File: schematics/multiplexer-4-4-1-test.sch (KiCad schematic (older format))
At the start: 10 parts

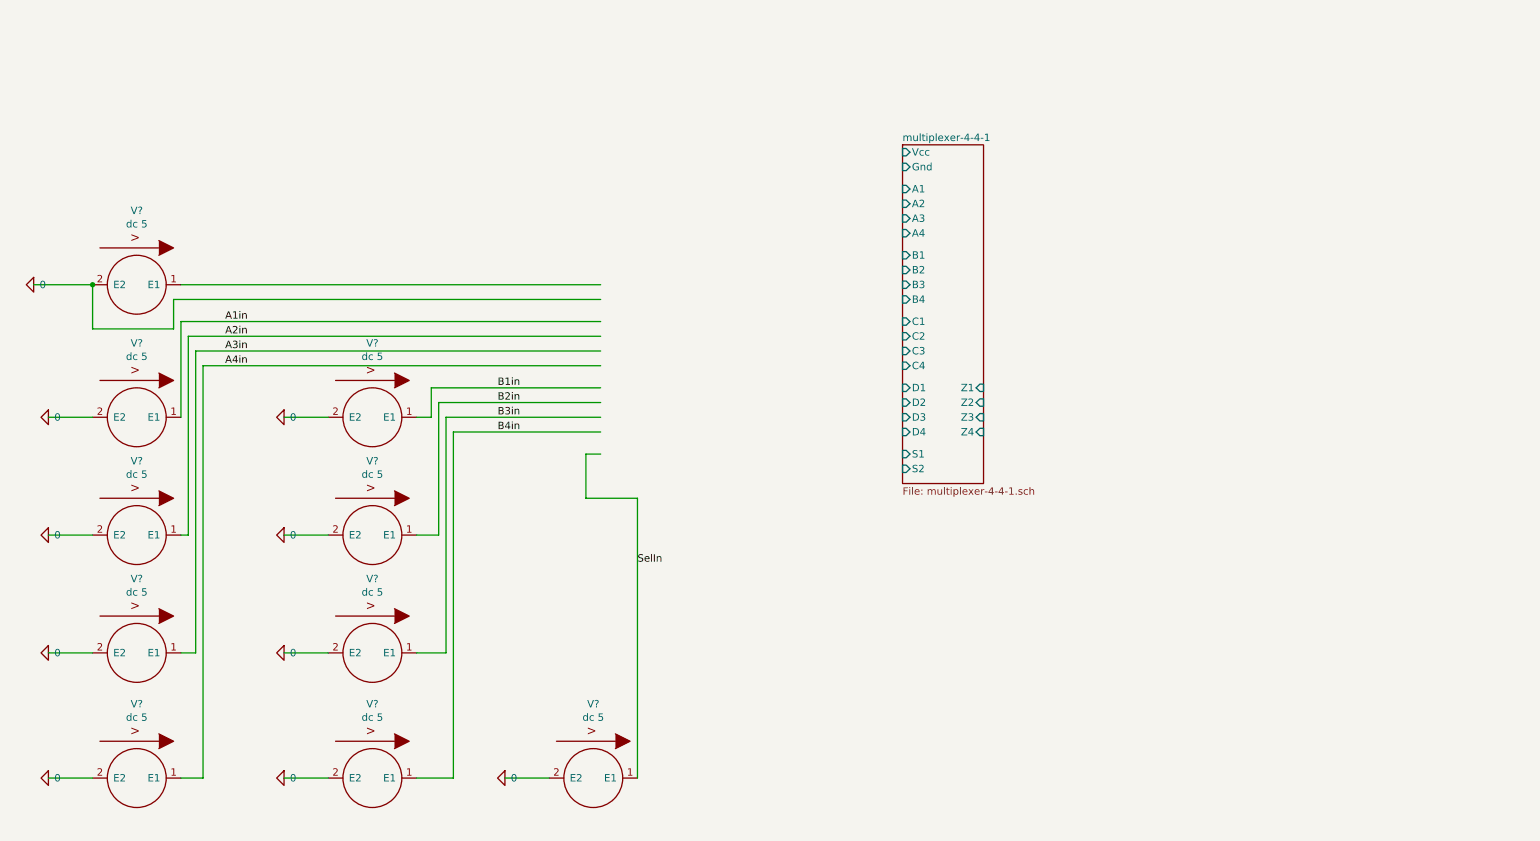
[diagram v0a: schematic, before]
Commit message: Adds a test for the 4-4-1 multiplexer
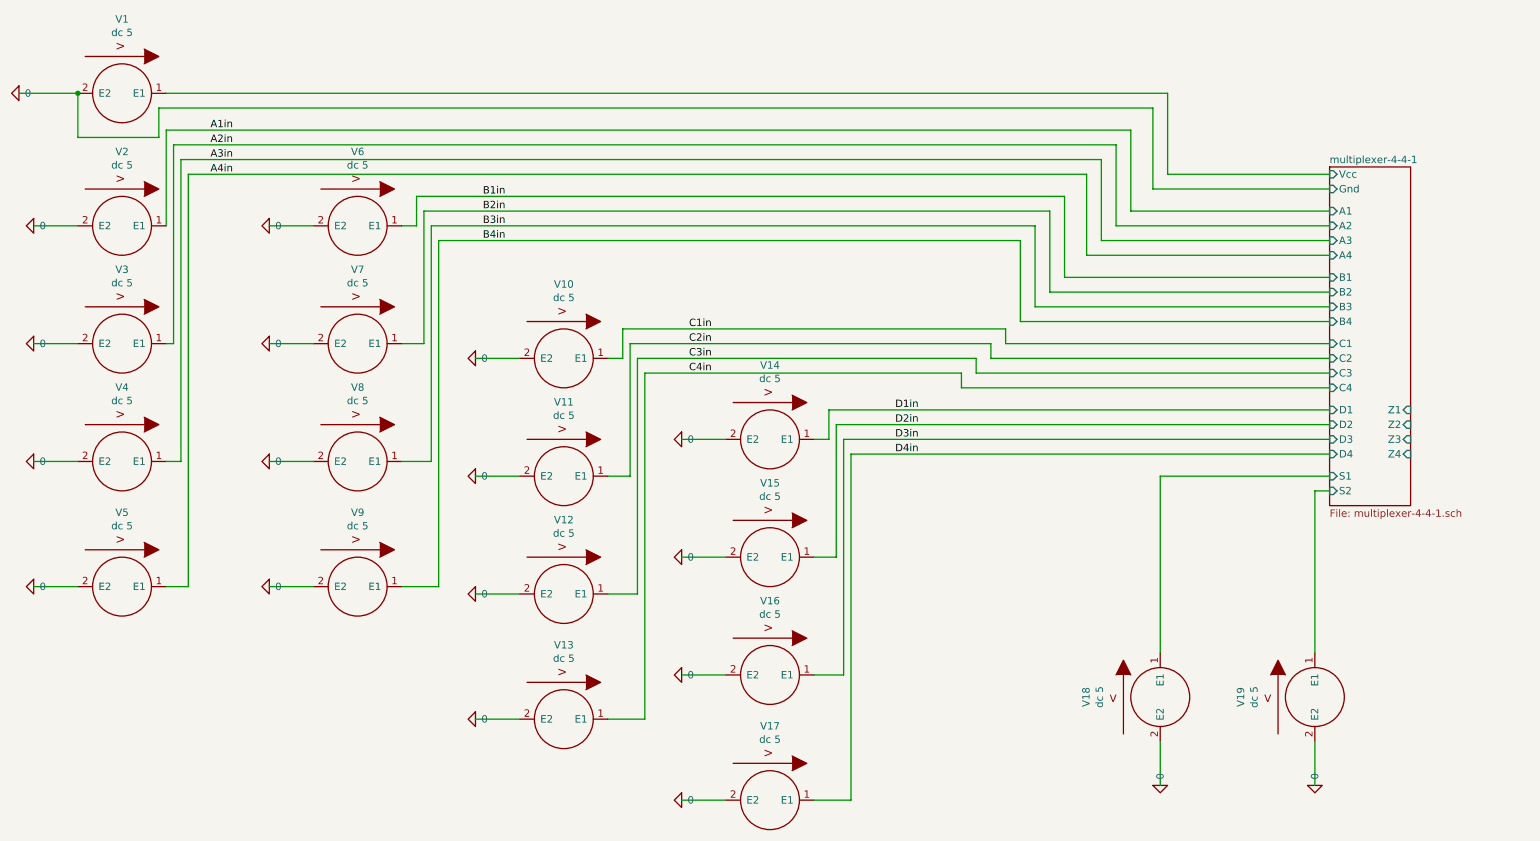
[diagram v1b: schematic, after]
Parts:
- added V10, V11, V12, V13, V14, V15, V16, V17, V19: dc 5, symbol pspice:VSOURCE
- gave numbers to parts that had none: 10
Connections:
- net labels added: C1in, C2in, C3in, C4in, D1in, D2in, D3in, D4in
- net labels removed: SelIn
- wire segments 42 -> 103
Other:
- moved on the sheet: V1, V18, V2, V3, V4, V5, V6, V7, V8, V9

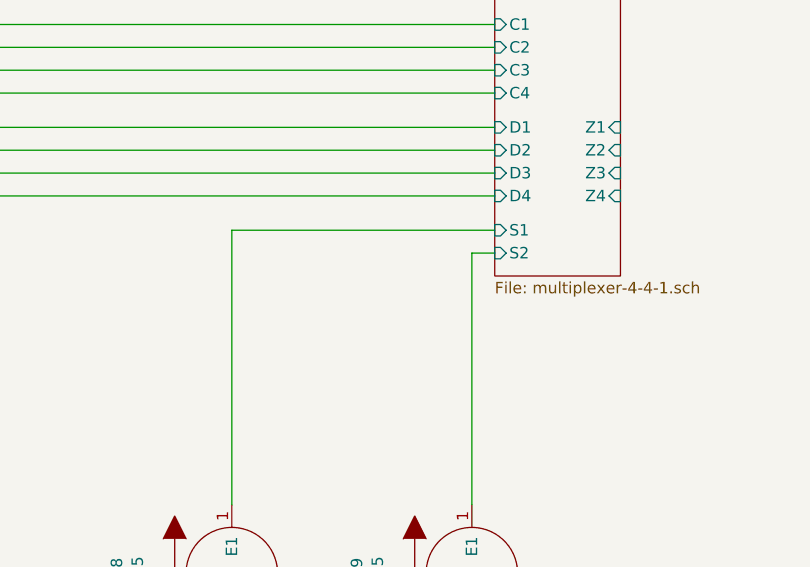
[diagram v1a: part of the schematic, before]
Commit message: More testing.  Trying to find defect in ALU
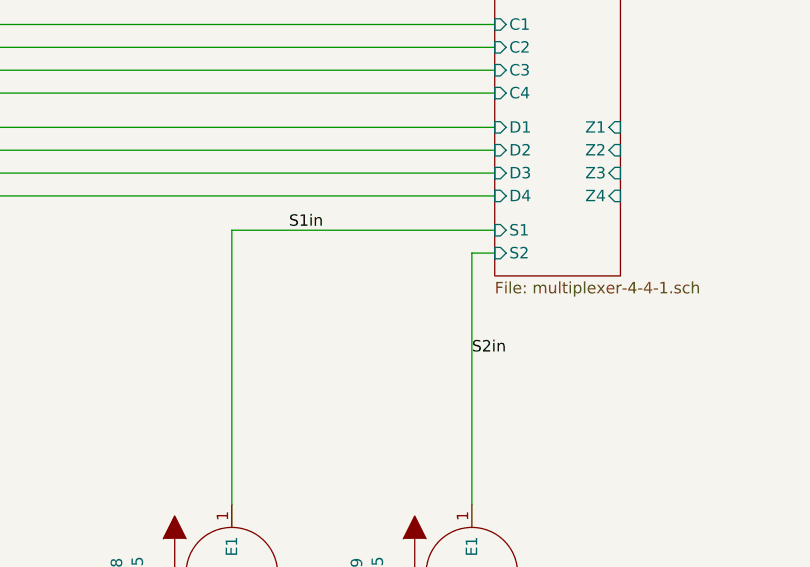
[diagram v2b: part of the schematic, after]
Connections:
- net multiplexer-4-4-1/S1 renamed S1in
- net multiplexer-4-4-1/S2 renamed S2in
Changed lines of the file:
@@
 EESchema Schematic File Version 4
+LIBS:multiplexer-4-4-1-test-cache
 EELAYER 26 0
 EELAYER END
@@
 P 950 1400
 AR Path="/5C44C753/5C44D98D" Ref="#GND?"  Part="1"
-AR Path="/5C44D98D" Ref="#GND0101"  Part="1"
-F 0 "#GND0101" H 950 1300 50  0001 C CNN
+AR Path="/5C44D98D" Ref="#GND01"  Part="1"
+F 0 "#GND01" H 950 1300 50  0001 C CNN
 F 1 "0" V 950 1440 50  0000 L CNN
 F 2 "" H 950 1400 50  0001 C CNN
@@
 P 1050 2300
 AR Path="/5C44C753/5C44D9A0" Ref="#GND?"  Part="1"
-AR Path="/5C44D9A0" Ref="#GND0102"  Part="1"
-F 0 "#GND0102" H 1050 2200 50  0001 C CNN
+AR Path="/5C44D9A0" Ref="#GND02"  Part="1"
+F 0 "#GND02" H 1050 2200 50  0001 C CNN
 F 1 "0" V 1050 2340 50  0000 L CNN
 F 2 "" H 1050 2300 50  0001 C CNN
@@
 P 1050 3100
 AR Path="/5C44C753/5C44D9AE" Ref="#GND?"  Part="1"
-AR Path="/5C44D9AE" Ref="#GND0103"  Part="1"
-F 0 "#GND0103" H 1050 3000 50  0001 C CNN
+AR Path="/5C44D9AE" Ref="#GND03"  Part="1"
+F 0 "#GND03" H 1050 3000 50  0001 C CNN
 F 1 "0" V 1050 3140 50  0000 L CNN
 F 2 "" H 1050 3100 50  0001 C CNN
@@
 P 1050 3900
 AR Path="/5C44C753/5C44D9BC" Ref="#GND?"  Part="1"
-AR Path="/5C44D9BC" Ref="#GND0104"  Part="1"
-F 0 "#GND0104" H 1050 3800 50  0001 C CNN
+AR Path="/5C44D9BC" Ref="#GND04"  Part="1"
+F 0 "#GND04" H 1050 3800 50  0001 C CNN
 F 1 "0" V 1050 3940 50  0000 L CNN
 F 2 "" H 1050 3900 50  0001 C CNN
@@
 P 1050 4750
 AR Path="/5C44C753/5C44D9CA" Ref="#GND?"  Part="1"
-AR Path="/5C44D9CA" Ref="#GND0105"  Part="1"
-F 0 "#GND0105" H 1050 4650 50  0001 C CNN
+AR Path="/5C44D9CA" Ref="#GND05"  Part="1"
+F 0 "#GND05" H 1050 4650 50  0001 C CNN
 F 1 "0" V 1050 4790 50  0000 L CNN
 F 2 "" H 1050 4750 50  0001 C CNN
@@
 P 2650 4750
 AR Path="/5C44C753/5C44D9D8" Ref="#GND?"  Part="1"
-AR Path="/5C44D9D8" Ref="#GND0106"  Part="1"
-F 0 "#GND0106" H 2650 4650 50  0001 C CNN
+AR Path="/5C44D9D8" Ref="#GND09"  Part="1"
+F 0 "#GND09" H 2650 4650 50  0001 C CNN
 F 1 "0" V 2650 4790 50  0000 L CNN
 F 2 "" H 2650 4750 50  0001 C CNN
@@
 P 2650 3900
 AR Path="/5C44C753/5C44D9E6" Ref="#GND?"  Part="1"
-AR Path="/5C44D9E6" Ref="#GND0107"  Part="1"
-F 0 "#GND0107" H 2650 3800 50  0001 C CNN
+AR Path="/5C44D9E6" Ref="#GND08"  Part="1"
+F 0 "#GND08" H 2650 3800 50  0001 C CNN
 F 1 "0" V 2650 3940 50  0000 L CNN
 F 2 "" H 2650 3900 50  0001 C CNN
@@
 P 2650 3100
 AR Path="/5C44C753/5C44D9F4" Ref="#GND?"  Part="1"
-AR Path="/5C44D9F4" Ref="#GND0108"  Part="1"
-F 0 "#GND0108" H 2650 3000 50  0001 C CNN
+AR Path="/5C44D9F4" Ref="#GND07"  Part="1"
+F 0 "#GND07" H 2650 3000 50  0001 C CNN
 F 1 "0" V 2650 3140 50  0000 L CNN
 F 2 "" H 2650 3100 50  0001 C CNN
@@
 P 2650 2300
 AR Path="/5C44C753/5C44DA02" Ref="#GND?"  Part="1"
-AR Path="/5C44DA02" Ref="#GND0109"  Part="1"
-F 0 "#GND0109" H 2650 2200 50  0001 C CNN
+AR Path="/5C44DA02" Ref="#GND06"  Part="1"
+F 0 "#GND06" H 2650 2200 50  0001 C CNN
 F 1 "0" V 2650 2340 50  0000 L CNN
 F 2 "" H 2650 2300 50  0001 C CNN
@@
 P 8700 6100
 AR Path="/5C44C753/5C44DA10" Ref="#GND?"  Part="1"
-AR Path="/5C44DA10" Ref="#GND0110"  Part="1"
-F 0 "#GND0110" H 8700 6000 50  0001 C CNN
+AR Path="/5C44DA10" Ref="#GND018"  Part="1"
+F 0 "#GND018" H 8700 6000 50  0001 C CNN
 F 1 "0" V 8700 6140 50  0000 L CNN
 F 2 "" H 8700 6100 50  0001 C CNN
@@
 P 4050 5650
 AR Path="/5C44C753/5C4656F5" Ref="#GND?"  Part="1"
-AR Path="/5C4656F5" Ref="#GND0111"  Part="1"
-F 0 "#GND0111" H 4050 5550 50  0001 C CNN
+AR Path="/5C4656F5" Ref="#GND013"  Part="1"
+F 0 "#GND013" H 4050 5550 50  0001 C CNN
 F 1 "0" V 4050 5690 50  0000 L CNN
 F 2 "" H 4050 5650 50  0001 C CNN
@@
 P 4050 4800
 AR Path="/5C44C753/5C465703" Ref="#GND?"  Part="1"
-AR Path="/5C465703" Ref="#GND0112"  Part="1"
-F 0 "#GND0112" H 4050 4700 50  0001 C CNN
+AR Path="/5C465703" Ref="#GND012"  Part="1"
+F 0 "#GND012" H 4050 4700 50  0001 C CNN
 F 1 "0" V 4050 4840 50  0000 L CNN
 F 2 "" H 4050 4800 50  0001 C CNN
@@
 P 4050 4000
 AR Path="/5C44C753/5C465711" Ref="#GND?"  Part="1"
-AR Path="/5C465711" Ref="#GND0113"  Part="1"
-F 0 "#GND0113" H 4050 3900 50  0001 C CNN
+AR Path="/5C465711" Ref="#GND011"  Part="1"
+F 0 "#GND011" H 4050 3900 50  0001 C CNN
 F 1 "0" V 4050 4040 50  0000 L CNN
 F 2 "" H 4050 4000 50  0001 C CNN
@@
 P 4050 3200
 AR Path="/5C44C753/5C46571F" Ref="#GND?"  Part="1"
-AR Path="/5C46571F" Ref="#GND0114"  Part="1"
-F 0 "#GND0114" H 4050 3100 50  0001 C CNN
+AR Path="/5C46571F" Ref="#GND010"  Part="1"
+F 0 "#GND010" H 4050 3100 50  0001 C CNN
 F 1 "0" V 4050 3240 50  0000 L CNN
 F 2 "" H 4050 3200 50  0001 C CNN
@@
 P 5450 6200
 AR Path="/5C44C753/5C467250" Ref="#GND?"  Part="1"
-AR Path="/5C467250" Ref="#GND0115"  Part="1"
-F 0 "#GND0115" H 5450 6100 50  0001 C CNN
+AR Path="/5C467250" Ref="#GND017"  Part="1"
+F 0 "#GND017" H 5450 6100 50  0001 C CNN
 F 1 "0" V 5450 6240 50  0000 L CNN
 F 2 "" H 5450 6200 50  0001 C CNN
@@
 P 5450 5350
 AR Path="/5C44C753/5C46725E" Ref="#GND?"  Part="1"
-AR Path="/5C46725E" Ref="#GND0116"  Part="1"
-F 0 "#GND0116" H 5450 5250 50  0001 C CNN
+AR Path="/5C46725E" Ref="#GND016"  Part="1"
+F 0 "#GND016" H 5450 5250 50  0001 C CNN
 F 1 "0" V 5450 5390 50  0000 L CNN
 F 2 "" H 5450 5350 50  0001 C CNN
@@
 P 5450 4550
 AR Path="/5C44C753/5C46726C" Ref="#GND?"  Part="1"
-AR Path="/5C46726C" Ref="#GND0117"  Part="1"
-F 0 "#GND0117" H 5450 4450 50  0001 C CNN
+AR Path="/5C46726C" Ref="#GND015"  Part="1"
+F 0 "#GND015" H 5450 4450 50  0001 C CNN
 F 1 "0" V 5450 4590 50  0000 L CNN
 F 2 "" H 5450 4550 50  0001 C CNN
@@
 P 5450 3750
 AR Path="/5C44C753/5C46727A" Ref="#GND?"  Part="1"
-AR Path="/5C46727A" Ref="#GND0118"  Part="1"
-F 0 "#GND0118" H 5450 3650 50  0001 C CNN
+AR Path="/5C46727A" Ref="#GND014"  Part="1"
+F 0 "#GND014" H 5450 3650 50  0001 C CNN
 F 1 "0" V 5450 3790 50  0000 L CNN
 F 2 "" H 5450 3750 50  0001 C CNN
@@
 P 9750 6100
 AR Path="/5C44C753/5C46EC47" Ref="#GND?"  Part="1"
-AR Path="/5C46EC47" Ref="#GND0119"  Part="1"
-F 0 "#GND0119" H 9750 6000 50  0001 C CNN
+AR Path="/5C46EC47" Ref="#GND019"  Part="1"
+F 0 "#GND019" H 9750 6000 50  0001 C CNN
 F 1 "0" V 9750 6140 50  0000 L CNN
 F 2 "" H 9750 6100 50  0001 C CNN
@@
 Wire Wire Line
 	8700 4000 8700 5200
+Text Label 8950 4000 0    50   ~ 0
+S1in
+Text Label 9750 4550 0    50   ~ 0
+S2in
 $EndSCHEMATC
